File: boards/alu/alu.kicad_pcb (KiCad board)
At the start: 2 copper layers, 90 x 100 mm, 70 parts, among them J1 61304021021, U1 SN74ACT08PW, U10 74ACT244MTC, U11 74ACT32MTCX, U12 MC74ACT138DTR2G, U13 SN74ACT08PW, U14 MC74ACT02DTR2G, U15 SN74ACT08PW, U16 74ACT244MTC, U17 74ACT244MTC, U18 74ACT244MTC, U19 74ACT244MTC, U2 SN74ACT08PW, U20 74ACT244MTC, U21 SN74ACT240PWR, U22 MC74ACT86DG, U23 MC74ACT86DG, U24 MC74ACT86DG, U25 MC74ACT86DG, U26 MC74ACT86DG, U27 MC74ACT86DG, U28 MC74ACT86DG, U29 MC74ACT86DG, U3 74ACT244MTC, U30 SN74ACT08PW, U31 SN74ACT08PW, U32 SN74ACT08PW, U33 SN74ACT08PW, U34 74ACT32MTCX, U35 74ACT32MTCX, U36 MC74ACT86DG, U37 MC74ACT02DTR2G, U38 SN74ACT08PW, U4 MC74AC157DR2G, U5 MC74AC157DR2G, U6 MC74AC157DR2G, U7 MC74AC157DR2G, U8 74ACT32MTCX, U9 74ACT32MTCX

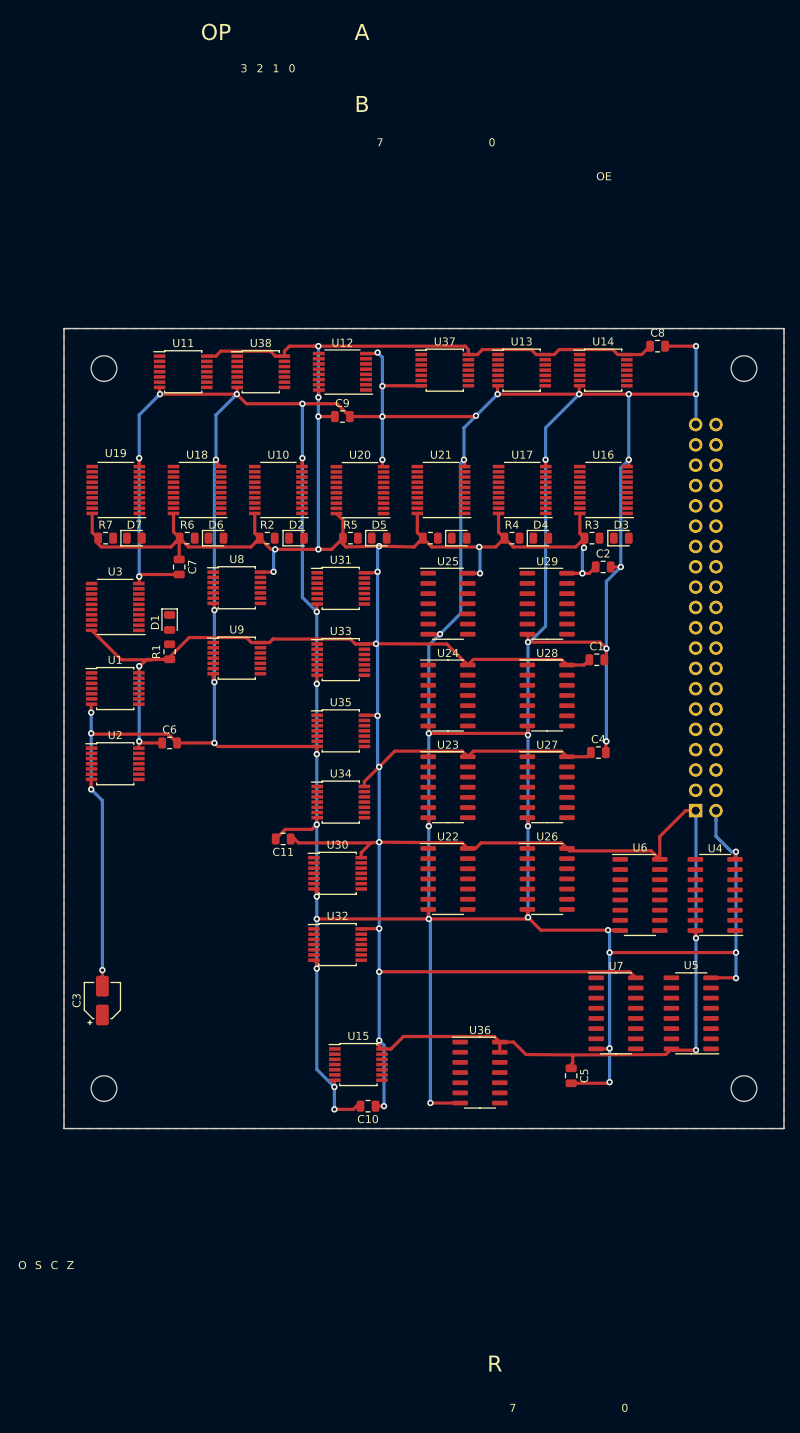
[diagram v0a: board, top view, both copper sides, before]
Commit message: ALU board complete
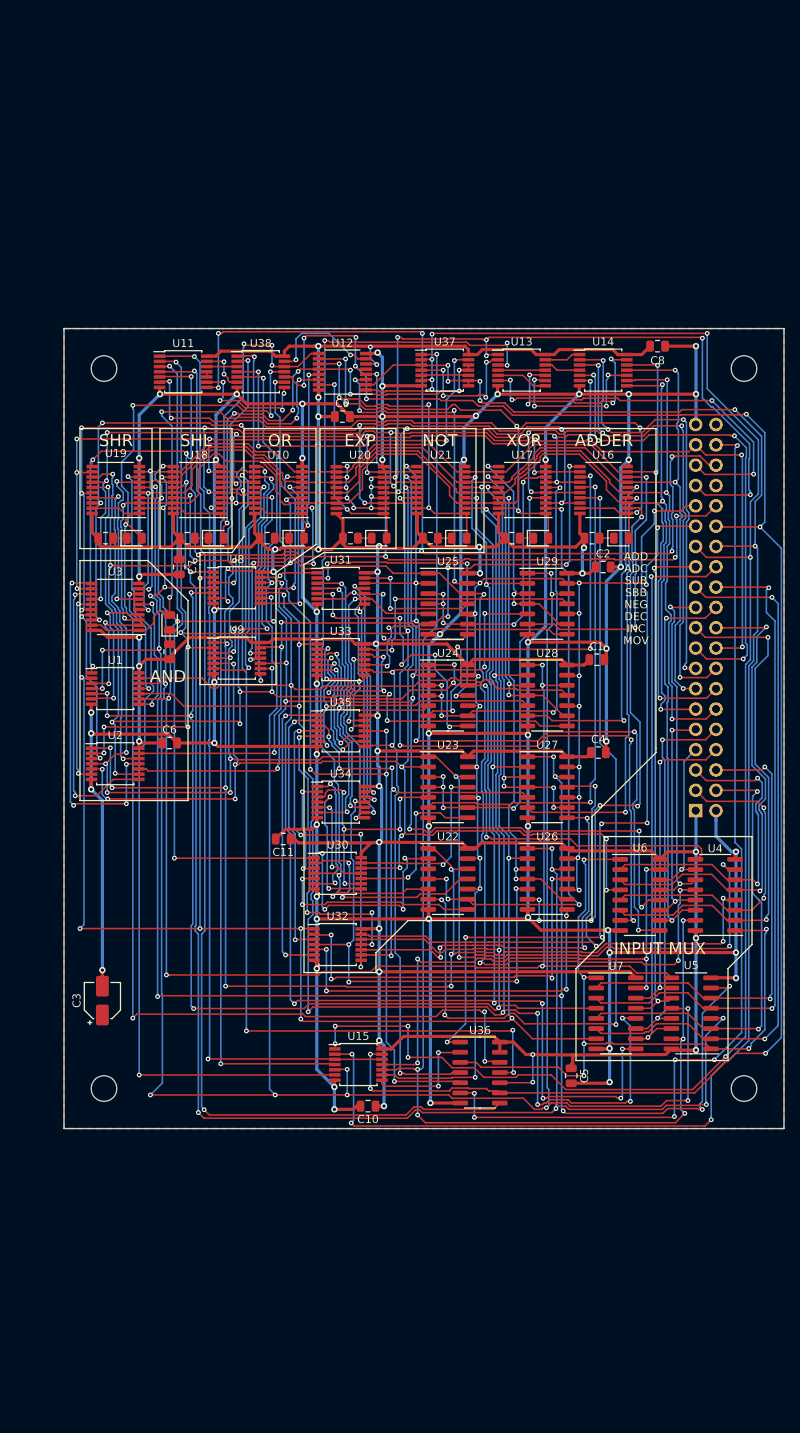
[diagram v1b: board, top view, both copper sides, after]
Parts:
- turned D1 to 90 degrees
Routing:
- net /sa7: track 0.00 -> 339.5 mm, vias 0 -> 13
- net /sa4: track 0.00 -> 244.2 mm, vias 0 -> 11
- net /adder_b7: track 0.00 -> 231.4 mm, vias 0 -> 12
- net /sa5: track 0.00 -> 228.7 mm, vias 0 -> 14
- net /adder_b4: track 0.00 -> 227.6 mm, vias 0 -> 9
- net /op3: track 0.00 -> 220.2 mm, vias 0 -> 10
- net /adder_b6: track 0.00 -> 219.5 mm, vias 0 -> 11
- net /op0: track 0.00 -> 213.9 mm, vias 0 -> 11
- net /adder_b5: track 0.00 -> 211.3 mm, vias 0 -> 9
- net /adder_sub: track 0.00 -> 210.4 mm, vias 0 -> 23
- net /op1: track 0.00 -> 207.5 mm, vias 0 -> 9
- net /sa1: track 0.00 -> 205.6 mm, vias 0 -> 12
- net /sa0: track 0.00 -> 198.6 mm, vias 0 -> 12
- net /sa3: track 0.00 -> 198.4 mm, vias 0 -> 11
- net /sa6: track 0.00 -> 197.6 mm, vias 0 -> 10
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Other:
- board text added: "ADC"
- board text added: "ADD"
- board text added: "ADDER"
- board text added: "AND"
- board text added: "DEC"
- board text added: "EXP"
- board text added: "INC"
- board text added: "INPUT MUX"
- board text added: "MOV"
- board text added: "NEG"
- board text added: "NOT"
- board text added: "OR"
- board text added: "SBB"
- board text added: "SHL"
- board text added: "SHR"
- board text added: "SUB"
- board text added: "XOR"
- board text removed: "0"
- board text removed: "1"
- board text removed: "2"
- board text removed: "3"
- board text removed: "7"
- board text removed: "A"
- board text removed: "B"
- board text removed: "C"
- board text removed: "O"
- board text removed: "OE"
- board text removed: "OP"
- board text removed: "R"
- board text removed: "S"
- board text removed: "Z"

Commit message: ALU board: change capacitor footprint, show labels
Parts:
- C3: footprint Capacitor_SMD:CP_Elec_4x4.5 -> Capacitor_Tantalum_SMD:CP_EIA-3528-21_Kemet-B_Pad1.50x2.35mm_HandSolder
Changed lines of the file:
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@@
   )
   (layers
-    (0 F.Cu signal hide)
-    (31 B.Cu signal hide)
+    (0 F.Cu signal)
+    (31 B.Cu signal)
     (32 B.Adhes user)
     (33 F.Adhes user)
@@
     (add_net VCC)
   )
+  (module Capacitor_Tantalum_SMD:CP_EIA-3528-21_Kemet-B_Pad1.50x2.35mm_HandSolder (layer F.Cu)
+    (at 114.8 134 90)
+    (descr "Tantalum Capacitor SMD Kemet-B (3528-21 Metric), IPC_7351 nominal, (Body size from: http://www.kemet.com/Lists/ProductCatalog/Attachments/253/KEM_TC101_STD.pdf), generated with kicad-footprint-generator")
+    (tags "capacitor tantalum")
+    (attr smd)
+    (fp_text reference C3 (at 0 -2.35 90) (layer F.SilkS)
+      (effects (font (size 1 1) (thickness 0.15)))
+    )
+    (fp_text value "10u x 6.3V" (at 0 2.35 90) (layer F.Fab)
+      (effects (font (size 1 1) (thickness 0.15)))
+    )
+    (fp_text user %R (at 0 0 90) (layer F.Fab)
+      (effects (font (size 0.88 0.88) (thickness 0.13)))
+    )
+    (fp_line (start 2.62 1.65) (end -2.62 1.65) (layer F.CrtYd) (width 0.05))
+    (fp_line (start 2.62 -1.65) (end 2.62 1.65) (layer F.CrtYd) (width 0.05))
+    (fp_line (start -2.62 -1.65) (end 2.62 -1.65) (layer F.CrtYd) (width 0.05))
+    (fp_line (start -2.62 1.65) (end -2.62 -1.65) (layer F.CrtYd) (width 0.05))
+    (fp_line (start -2.635 1.51) (end 1.75 1.51) (layer F.SilkS) (width 0.12))
+    (fp_line (start -2.635 -1.51) (end -2.635 1.51) (layer F.SilkS) (width 0.12))
+    (fp_line (start 1.75 -1.51) (end -2.635 -1.51) (layer F.SilkS) (width 0.12))
+    (fp_line (start 1.75 1.4) (end 1.75 -1.4) (layer F.Fab) (width 0.1))
+    (fp_line (start -1.75 1.4) (end 1.75 1.4) (layer F.Fab) (width 0.1))
+    (fp_line (start -1.75 -0.7) (end -1.75 1.4) (layer F.Fab) (width 0.1))
+    (fp_line (start -1.05 -1.4) (end -1.75 -0.7) (layer F.Fab) (width 0.1))
+    (fp_line (start 1.75 -1.4) (end -1.05 -1.4) (layer F.Fab) (width 0.1))
+    (pad 2 smd roundrect (at 1.625 0 90) (size 1.5 2.35) (layers F.Cu F.Paste F.Mask) (roundrect_rratio 0.166667)
+      (net 1 GND))
+    (pad 1 smd roundrect (at -1.625 0 90) (size 1.5 2.35) (layers F.Cu F.Paste F.Mask) (roundrect_rratio 0.166667)
+      (net 2 VCC))
+    (model ${KISYS3DMOD}/Capacitor_Tantalum_SMD.3dshapes/CP_EIA-3528-21_Kemet-B.wrl
+      (at (xyz 0 0 0))
+      (scale (xyz 1 1 1))
+      (rotate (xyz 0 0 0))
+    )
+  )
   (module Resistor_SMD:R_0805_2012Metric (layer F.Cu)
     (at 115.2 76.2)
@@
     (tags resistor)
     (attr smd)
-    (fp_text reference R7 (at 0 -1.65) (layer F.SilkS) hide
+    (fp_text reference R7 (at 0 -1.65) (layer F.SilkS)
       (effects (font (size 1 1) (thickness 0.15)))
     )
@@
     (tags resistor)
     (attr smd)
-    (fp_text reference R6 (at 0 -1.65) (layer F.SilkS) hide
+    (fp_text reference R6 (at 0 -1.65) (layer F.SilkS)
       (effects (font (size 1 1) (thickness 0.15)))
     )
@@
     (tags resistor)
     (attr smd)
-    (fp_text reference R5 (at 0 -1.65) (layer F.SilkS) hide
+    (fp_text reference R5 (at 0 -1.65) (layer F.SilkS)
       (effects (font (size 1 1) (thickness 0.15)))
     )
@@
     (tags resistor)
     (attr smd)
-    (fp_text reference R4 (at 0 -1.65) (layer F.SilkS) hide
+    (fp_text reference R4 (at 0 -1.65) (layer F.SilkS)
       (effects (font (size 1 1) (thickness 0.15)))
     )
@@
     (tags resistor)
     (attr smd)
-    (fp_text reference R3 (at 0 -1.65) (layer F.SilkS) hide
+    (fp_text reference R3 (at 0 -1.65) (layer F.SilkS)
       (effects (font (size 1 1) (thickness 0.15)))
     )
@@
     (tags resistor)
     (attr smd)
-    (fp_text reference R2 (at 0 -1.65) (layer F.SilkS) hide
+    (fp_text reference R2 (at 0 -1.65) (layer F.SilkS)
       (effects (font (size 1 1) (thickness 0.15)))
     )
@@
     (tags resistor)
     (attr smd)
-    (fp_text reference R1 (at 0 -1.65 90) (layer F.SilkS) hide
+    (fp_text reference R1 (at 0 -1.7 90) (layer F.SilkS)
       (effects (font (size 1 1) (thickness 0.15)))
     )
@@
     (tags diode)
     (attr smd)
-    (fp_text reference D7 (at 0 -1.65) (layer F.SilkS) hide
+    (fp_text reference D7 (at 0 -1.65) (layer F.SilkS)
       (effects (font (size 1 1) (thickness 0.15)))
     )
@@
     (tags diode)
     (attr smd)
-    (fp_text reference D6 (at 0 -1.65) (layer F.SilkS) hide
+    (fp_text reference D6 (at 0 -1.65) (layer F.SilkS)
       (effects (font (size 1 1) (thickness 0.15)))
     )
@@
     (tags diode)
     (attr smd)
-    (fp_text reference D5 (at 0 -1.65) (layer F.SilkS) hide
+    (fp_text reference D5 (at 0 -1.65) (layer F.SilkS)
       (effects (font (size 1 1) (thickness 0.15)))
     )
@@
     (tags diode)
     (attr smd)
-    (fp_text reference D4 (at 0 -1.65) (layer F.SilkS) hide
+    (fp_text reference D4 (at 0 -1.65) (layer F.SilkS)
       (effects (font (size 1 1) (thickness 0.15)))
     )
@@
     (tags diode)
     (attr smd)
-    (fp_text reference D3 (at 0 -1.65) (layer F.SilkS) hide
+    (fp_text reference D3 (at 0 -1.65) (layer F.SilkS)
       (effects (font (size 1 1) (thickness 0.15)))
     )
@@
     (tags diode)
     (attr smd)
-    (fp_text reference D2 (at 0 -1.65) (layer F.SilkS) hide
+    (fp_text reference D2 (at 0 -1.65) (layer F.SilkS)
       (effects (font (size 1 1) (thickness 0.15)))
     )
@@
     (tags diode)
     (attr smd)
-    (fp_text reference D1 (at 0 1.8 90) (layer F.SilkS) hide
+    (fp_text reference D1 (at 0 -1.7 90) (layer F.SilkS)
       (effects (font (size 1 1) (thickness 0.15)))
     )
@@
     (tags resistor)
     (attr smd)
-    (fp_text reference R8 (at 0 -1.65) (layer F.SilkS) hide
+    (fp_text reference R8 (at 0 -1.65) (layer F.SilkS)
       (effects (font (size 1 1) (thickness 0.15)))
     )
@@
     (tags diode)
     (attr smd)
-    (fp_text reference D8 (at 0 -1.65) (layer F.SilkS) hide
+    (fp_text reference D8 (at 0 -1.65) (layer F.SilkS)
       (effects (font (size 1 1) (thickness 0.15)))
     )
@@
       (at (xyz 0 0 0))
       (scale (xyz 1 1 1))
-      (rotate (xyz 0 0 0))
-    )
-  )
-  (module Capacitor_SMD:CP_Elec_4x4.5 (layer F.Cu)
-    (at 114.8 134 90)
-    (descr "SMD capacitor, aluminum electrolytic, Nichicon, 4.0x4.5mm")
-    (tags "capacitor electrolytic")
-    (attr smd)
-    (fp_text reference C3 (at 0 -3.2 90) (layer F.SilkS)
-      (effects (font (size 1 1) (thickness 0.15)))
-    )
-    (fp_text value "10u x 6.3V" (at 0 3.2 90) (layer F.Fab)
-      (effects (font (size 1 1) (thickness 0.15)))
-    )
-    (fp_circle (center 0 0) (end 2 0) (layer F.Fab) (width 0.1))
-    (fp_line (start 2.15 -2.15) (end 2.15 2.15) (layer F.Fab) (width 0.1))
-    (fp_line (start -1.15 -2.15) (end 2.15 -2.15) (layer F.Fab) (width 0.1))
-    (fp_line (start -1.15 2.15) (end 2.15 2.15) (layer F.Fab) (width 0.1))
-    (fp_line (start -2.15 -1.15) (end -2.15 1.15) (layer F.Fab) (width 0.1))
-    (fp_line (start -2.15 -1.15) (end -1.15 -2.15) (layer F.Fab) (width 0.1))
-    (fp_line (start -2.15 1.15) (end -1.15 2.15) (layer F.Fab) (width 0.1))
-    (fp_line (start -1.574773 -1) (end -1.174773 -1) (layer F.Fab) (width 0.1))
-    (fp_line (start -1.374773 -1.2) (end -1.374773 -0.8) (layer F.Fab) (width 0.1))
-    (fp_line (start 2.26 2.26) (end 2.26 1.06) (layer F.SilkS) (width 0.12))
-    (fp_line (start 2.26 -2.26) (end 2.26 -1.06) (layer F.SilkS) (width 0.12))
-    (fp_line (start -1.195563 -2.26) (end 2.26 -2.26) (layer F.SilkS) (width 0.12))
-    (fp_line (start -1.195563 2.26) (end 2.26 2.26) (layer F.SilkS) (width 0.12))
-    (fp_line (start -2.26 1.195563) (end -2.26 1.06) (layer F.SilkS) (width 0.12))
-    (fp_line (start -2.26 -1.195563) (end -2.26 -1.06) (layer F.SilkS) (width 0.12))
-    (fp_line (start -2.26 -1.195563) (end -1.195563 -2.26) (layer F.SilkS) (width 0.12))
-    (fp_line (start -2.26 1.195563) (end -1.195563 2.26) (layer F.SilkS) (width 0.12))
-    (fp_line (start -3 -1.56) (end -2.5 -1.56) (layer F.SilkS) (width 0.12))
-    (fp_line (start -2.75 -1.81) (end -2.75 -1.31) (layer F.SilkS) (width 0.12))
-    (fp_line (start 2.4 -2.4) (end 2.4 -1.05) (layer F.CrtYd) (width 0.05))
-    (fp_line (start 2.4 -1.05) (end 3.35 -1.05) (layer F.CrtYd) (width 0.05))
-    (fp_line (start 3.35 -1.05) (end 3.35 1.05) (layer F.CrtYd) (width 0.05))
-    (fp_line (start 3.35 1.05) (end 2.4 1.05) (layer F.CrtYd) (width 0.05))
-    (fp_line (start 2.4 1.05) (end 2.4 2.4) (layer F.CrtYd) (width 0.05))
-    (fp_line (start -1.25 2.4) (end 2.4 2.4) (layer F.CrtYd) (width 0.05))
-    (fp_line (start -1.25 -2.4) (end 2.4 -2.4) (layer F.CrtYd) (width 0.05))
-    (fp_line (start -2.4 1.25) (end -1.25 2.4) (layer F.CrtYd) (width 0.05))
-    (fp_line (start -2.4 -1.25) (end -1.25 -2.4) (layer F.CrtYd) (width 0.05))
-    (fp_line (start -2.4 -1.25) (end -2.4 -1.05) (layer F.CrtYd) (width 0.05))
-    (fp_line (start -2.4 1.05) (end -2.4 1.25) (layer F.CrtYd) (width 0.05))
-    (fp_line (start -2.4 -1.05) (end -3.35 -1.05) (layer F.CrtYd) (width 0.05))
-    (fp_line (start -3.35 -1.05) (end -3.35 1.05) (layer F.CrtYd) (width 0.05))
-    (fp_line (start -3.35 1.05) (end -2.4 1.05) (layer F.CrtYd) (width 0.05))
-    (fp_text user %R (at 0 0 90) (layer F.Fab)
-      (effects (font (size 0.8 0.8) (thickness 0.12)))
-    )
-    (pad 1 smd roundrect (at -1.8 0 90) (size 2.6 1.6) (layers F.Cu F.Paste F.Mask) (roundrect_rratio 0.15625)
-      (net 2 VCC))
-    (pad 2 smd roundrect (at 1.8 0 90) (size 2.6 1.6) (layers F.Cu F.Paste F.Mask) (roundrect_rratio 0.15625)
-      (net 1 GND))
-    (model ${KISYS3DMOD}/Capacitor_SMD.3dshapes/CP_Elec_4x4.5.wrl
-      (at (xyz 0 0 0))
-      (scale (xyz 1 1 1))

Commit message: ALU board: add PCB text
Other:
- board text added: "ALU rev.2"
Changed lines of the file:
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@@
   (general
     (thickness 1.6)
-    (drawings 82)
+    (drawings 83)
     (tracks 5166)
     (zones 0)
@@
     )
   )
+  (gr_text "ALU rev.2" (at 124.5 120) (layer F.Cu)
+    (effects (font (size 1.5 1.5) (thickness 0.3)))
+  )
   (gr_line (start 177.5 113.5) (end 177.5 126.5) (layer F.SilkS) (width 0.12))
